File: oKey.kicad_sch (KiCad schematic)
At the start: 24 parts, among them P1 USB_C_Plug_USB2.0, SW1 SW_Push, U1 RP2350_60QFN, U2 NCP1117-3.3_SOT223, U3 W25Q128JVS

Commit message: minimal schematic
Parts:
- added C16, C17: 15p, symbol Device:C
- added C18: 4.7u, symbol Device:C
- added C19: C, symbol Device:C
- added L1: 3.3u, symbol Device:L
- added R4: 0, symbol Device:R
- added R6: DNF, symbol Device:R
- added R7, R8: 1K, symbol Device:R
- added R9: 33, symbol Device:R
- added SW2: SW_Push, symbol Switch:SW_Push
- added X1: ABM8-272-T3, ABM8-272-T3_ABR, symbol ABM8-272-T3:ABM8-272-T3
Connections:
- net GND is gone; now on net +3V3: C1.1, C10.2, C11.2, C12.2, C13.2, C14.2, C15.2, C2.1, C3.2, C4.2, C5.2, C6.2, C7.2, C8.2, C9.2, P1.A1 (GND), P1.A12 (GND), P1.B1 (GND), P1.B12 (GND), P1.S1 (SHIELD), R1.2, SW1.2, U1.1 (IOVDD), U1.11 (IOVDD), U1.20 (IOVDD), U1.30 (IOVDD), U1.38 (IOVDD), U1.44 (ADC_AVDD), U1.45 (IOVDD), U1.53 (USB_OTP_VDD), U1.54 (QSPI_IOVDD), U2.1 (GND), U3.4 (GND)
- net +1V1: now also U1.50 (VREG_FB), C19.1, L1.1
- net +3V3: now also U1.47 (VREG_PGND), U1.49 (VREG_VIN), U1.61 (GND), C16.2, C17.2, C18.1, C19.2, R6.1, R9.1, SW2.2, X1.2, X1.4
- net XIN: now reaches U1.21 (XIN)
- net XIN: now also C16.1, X1.1
- net XOUT: now reaches U1.22 (XOUT)
- net XOUT: now also R7.2
- net at U1.26 (RUN): now also R8.2
- net at U1.46 (VREG_AVDD): now also C18.2, R9.2
- net at U1.48 (VREG_LX): now also L1.2
- net QSPI_SS: now reaches R5.2, U1.60 (QSPI_SS)
- net QSPI_SS: now also R4.1
- net at U3.1 (~{CS}): now also R4.2, R6.2
- new net: C17.1, R7.1, X1.3
- new net: R8.1, SW2.1
- no-connect marks 0 -> 34
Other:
- note added: "12 MHz Crystal"
- note added: "RESET"
- note added: "pullup that this flash chip doesn't need"
- moved on the sheet: R5, SW1

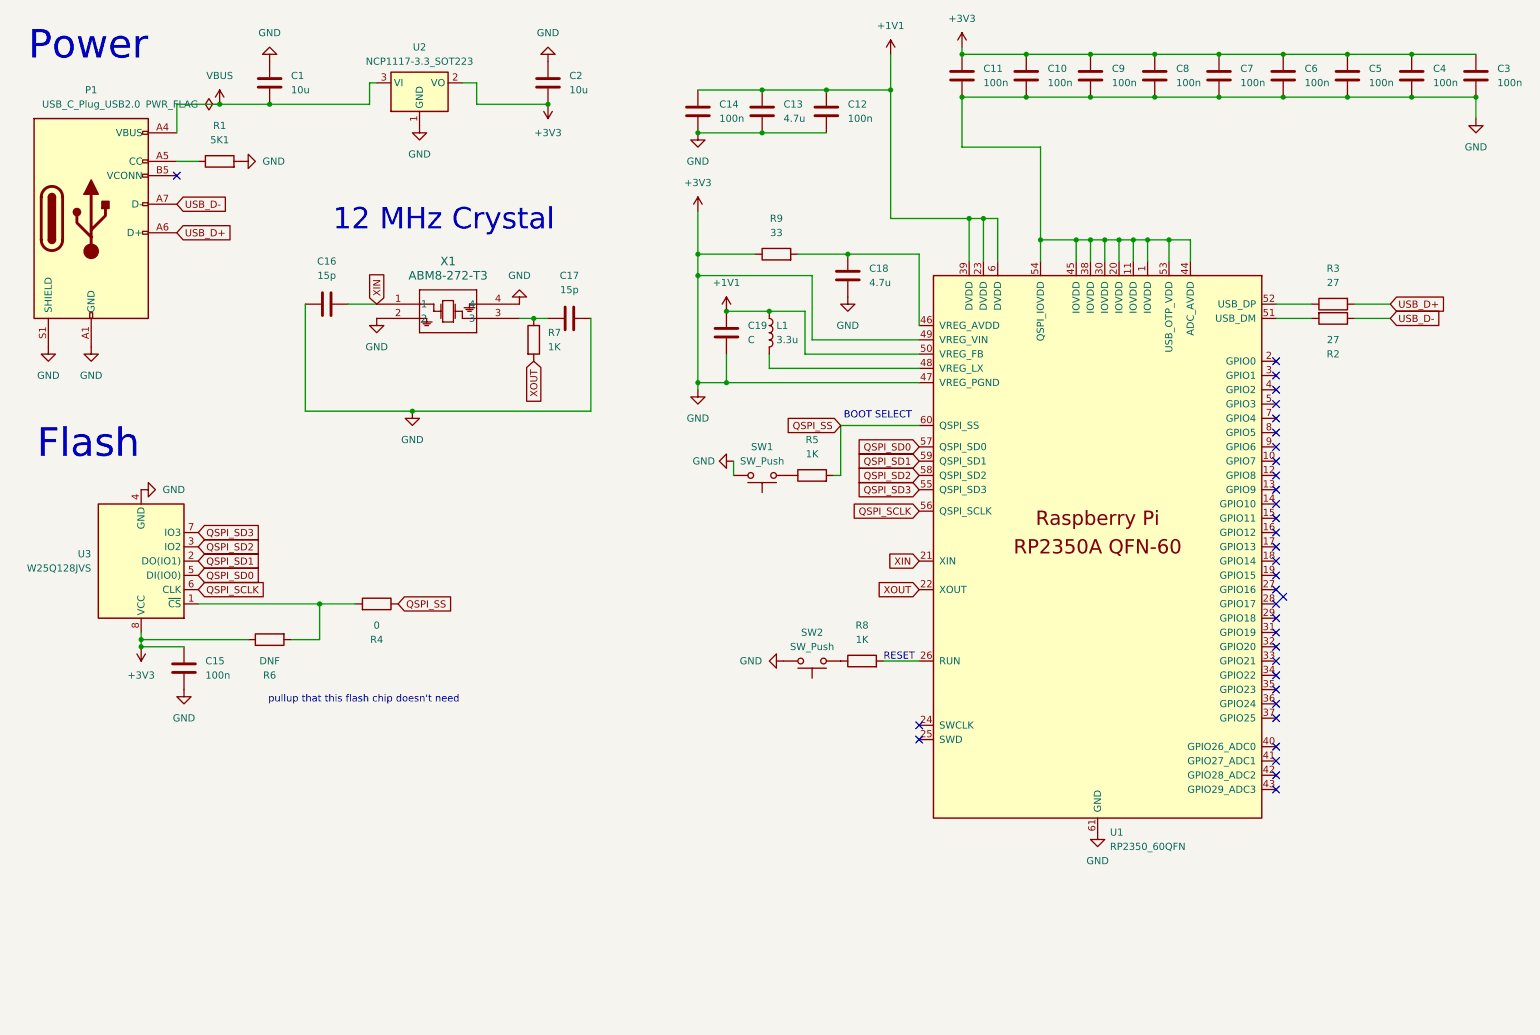
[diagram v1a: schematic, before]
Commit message: reorganise schematic and update images
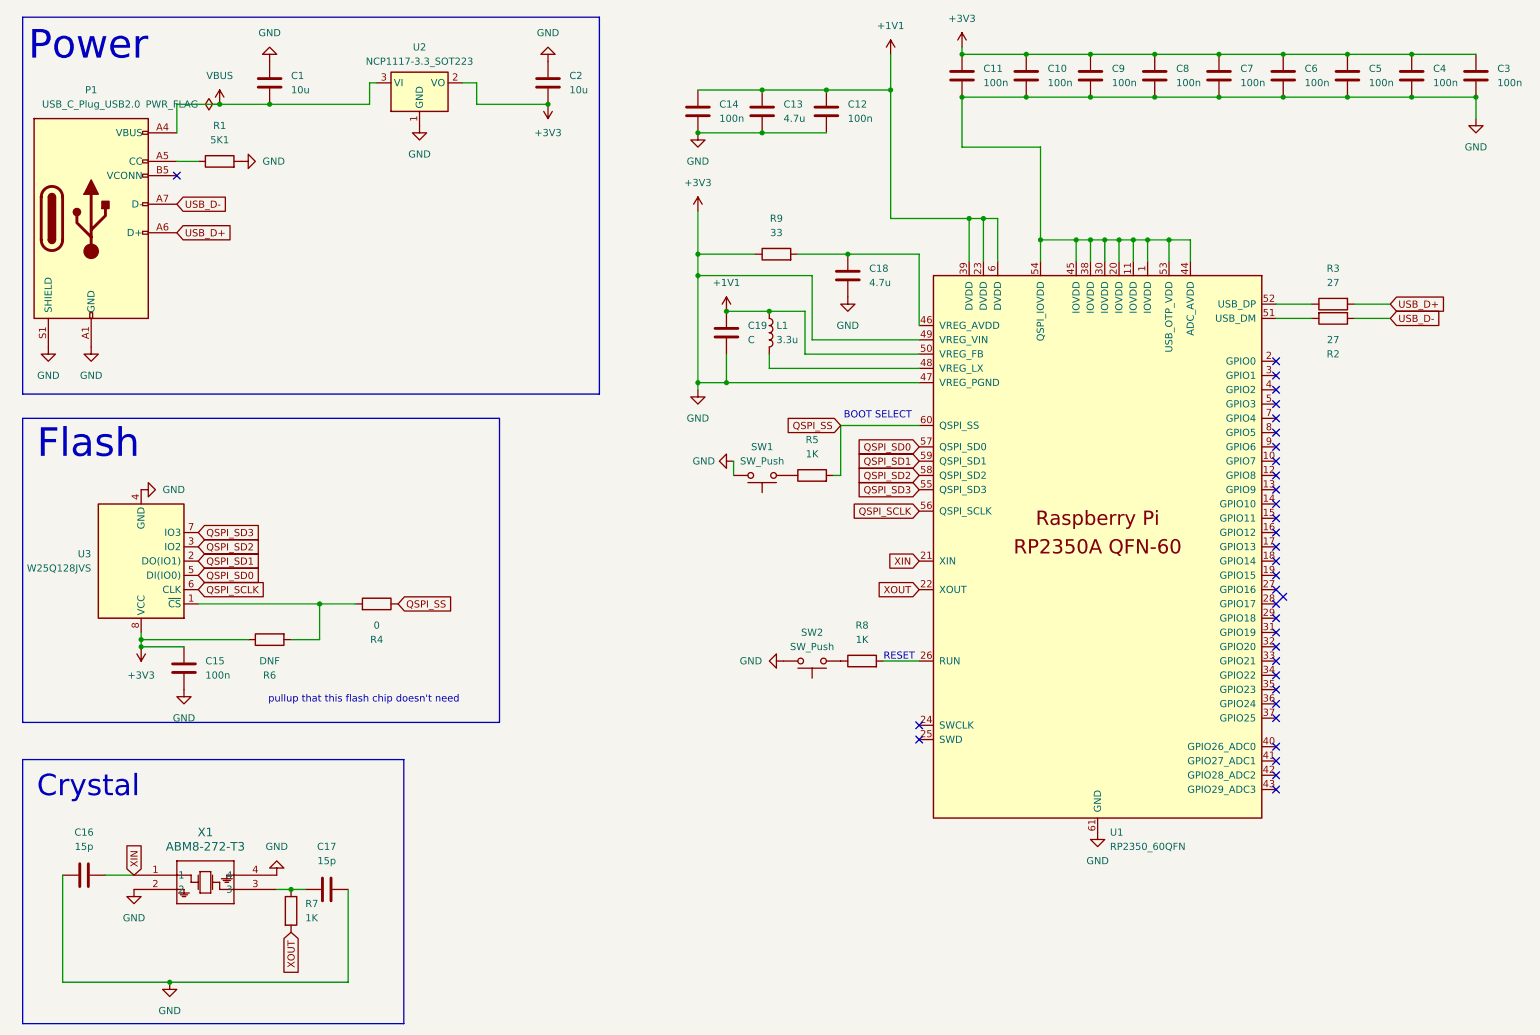
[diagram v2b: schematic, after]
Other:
- note added: "Crystal"
- note removed: "12 MHz Crystal"
- moved on the sheet: C16, C17, R7, X1
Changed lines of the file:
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@@
 	)
 	(junction
-		(at 105.41 68.58)
+		(at 62.23 170.18)
 		(diameter 0)
 		(color 0 0 0 0)
@@
 	)
 	(junction
-		(at 83.82 85.09)
+		(at 40.64 186.69)
 		(diameter 0)
 		(color 0 0 0 0)
@@
 	(wire
 		(pts
-			(xy 102.87 68.58) (xy 105.41 68.58)
+			(xy 59.69 170.18) (xy 62.23 170.18)
 		)
 		(stroke
@@
 	(wire
 		(pts
-			(xy 64.77 85.09) (xy 83.82 85.09)
+			(xy 21.59 186.69) (xy 40.64 186.69)
 		)
 		(stroke
@@
 	(wire
 		(pts
-			(xy 115.57 85.09) (xy 83.82 85.09)
+			(xy 72.39 186.69) (xy 40.64 186.69)
 		)
 		(stroke
@@
 	(wire
 		(pts
-			(xy 105.41 68.58) (xy 107.95 68.58)
+			(xy 62.23 170.18) (xy 64.77 170.18)
 		)
 		(stroke
@@
 	(wire
 		(pts
-			(xy 64.77 66.04) (xy 64.77 85.09)
+			(xy 21.59 167.64) (xy 21.59 186.69)
 		)
 		(stroke
@@
 	(wire
 		(pts
-			(xy 115.57 68.58) (xy 115.57 85.09)
+			(xy 72.39 170.18) (xy 72.39 186.69)
 		)
 		(stroke
@@
 	(wire
 		(pts
-			(xy 72.39 66.04) (xy 77.47 66.04)
+			(xy 29.21 167.64) (xy 34.29 167.64)
 		)
 		(stroke
@@
 		)
 	)
+	(rectangle
+		(start 14.478 14.986)
+		(end 117.094 82.042)
+		(stroke
+			(width 0)
+			(type default)
+		)
+		(fill
+			(type none)
+		)
+	)
+	(rectangle
+		(start 14.478 147.066)
+		(end 82.296 194.056)
+		(stroke
+			(width 0)
+			(type default)
+		)
+		(fill
+			(type none)
+		)
+	)
+	(rectangle
+		(start 14.478 86.36)
+		(end 99.314 140.462)
+		(stroke
+			(width 0)
+			(type default)
+		)
+		(fill
+			(type none)
+		)
+	)
 	(text "BOOT SELECT"
 		(exclude_from_sim no)
@@
 		)
 	)
-	(text "12 MHz Crystal"
+	(text "Crystal"
 		(exclude_from_sim no)
-		(at 89.408 51.054 0)
+		(at 26.162 151.892 0)
 		(effects
 			(font
@@
 	(global_label "XIN"
 		(shape input)
-		(at 77.47 66.04 90)
+		(at 34.29 167.64 90)
 		(fields_autoplaced yes)
 		(effects
@@
 		)
 		(property "Intersheetrefs" "${INTERSHEET_REFS}"
-			(at 77.47 59.91 90)
+			(at 34.29 161.51 90)
 			(effects
 				(font
@@
 	(global_label "XOUT"
 		(shape input)
-		(at 105.41 76.2 270)
+		(at 62.23 177.8 270)
 		(fields_autoplaced yes)
 		(effects
@@
 		)
 		(property "Intersheetrefs" "${INTERSHEET_REFS}"
-			(at 105.41 84.0233 90)
+			(at 62.23 185.6233 90)
 			(effects
 				(font
@@
 	(symbol
 		(lib_id "Device:R")
-		(at 105.41 72.39 0)
+		(at 62.23 173.99 0)
 		(unit 1)
 		(exclude_from_sim no)
@@
 		(fields_autoplaced yes)
 		(property "Reference" "R7"
-			(at 107.95 71.1199 0)
+			(at 64.77 172.7199 0)
 			(effects
 				(font
@@
 		)
 		(property "Value" "1K"
-			(at 107.95 73.6599 0)
+			(at 64.77 175.2599 0)
 			(effects
 				(font
@@
 		)
 		(property "Footprint" ""
-			(at 103.632 72.39 90)
+			(at 60.452 173.99 90)
 			(effects
 				(font
@@
 		)
 		(property "Datasheet" "~"
-			(at 105.41 72.39 0)
+			(at 62.23 173.99 0)
 			(effects
 				(font
@@
 		)
 		(property "Description" "Resistor"
-			(at 105.41 72.39 0)
+			(at 62.23 173.99 0)
 			(effects
 				(font
@@
 	(symbol
 		(lib_id "Device:C")
-		(at 68.58 66.04 270)
+		(at 25.4 167.64 270)
 		(unit 1)
 		(exclude_from_sim no)
@@
 		(fields_autoplaced yes)
 		(property "Reference" "C16"
-			(at 68.58 58.42 90)
+			(at 25.4 160.02 90)
 			(effects
 				(font
@@
 		)
 		(property "Value" "15p"
-			(at 68.58 60.96 90)
+			(at 25.4 162.56 90)
 			(effects
 				(font
@@
 		)
 		(property "Footprint" ""
-			(at 64.77 67.0052 0)
+			(at 21.59 168.6052 0)
 			(effects
 				(font
@@
 		)
 		(property "Datasheet" "~"
-			(at 68.58 66.04 0)
+			(at 25.4 167.64 0)
 			(effects
 				(font
@@
 		)
 		(property "Description" "Unpolarized capacitor"
-			(at 68.58 66.04 0)
+			(at 25.4 167.64 0)
 			(effects
 				(font
@@
 	(symbol
 		(lib_id "power:GND")
-		(at 77.47 68.58 0)
+		(at 34.29 170.18 0)
 		(unit 1)
 		(exclude_from_sim no)
@@
 		(fields_autoplaced yes)
 		(property "Reference" "#PWR017"
-			(at 77.47 74.93 0)
+			(at 34.29 176.53 0)
 			(effects
 				(font
@@
 		)
 		(property "Value" "GND"
-			(at 77.47 73.66 0)
+			(at 34.29 175.26 0)
 			(effects
 				(font
@@
 		)
 		(property "Footprint" ""
-			(at 77.47 68.58 0)
+			(at 34.29 170.18 0)
 			(effects
 				(font
@@
 		)
 		(property "Datasheet" ""
-			(at 77.47 68.58 0)
+			(at 34.29 170.18 0)
 			(effects
 				(font
@@
 		)
 		(property "Description" "Power symbol creates a global label with name \"GND\" , ground"
-			(at 77.47 68.58 0)
+			(at 34.29 170.18 0)
 			(effects
 				(font
@@
 	(symbol
 		(lib_id "power:GND")
-		(at 83.82 85.09 0)
+		(at 40.64 186.69 0)
 		(unit 1)
 		(exclude_from_sim no)
@@
 		(fields_autoplaced yes)
 		(property "Reference" "#PWR019"
-			(at 83.82 91.44 0)
+			(at 40.64 193.04 0)
 			(effects
 				(font
@@
 		)
 		(property "Value" "GND"
-			(at 83.82 90.17 0)
+			(at 40.64 191.77 0)
 			(effects
 				(font
@@
 		)
 		(property "Footprint" ""
-			(at 83.82 85.09 0)
+			(at 40.64 186.69 0)
 			(effects
 				(font
@@
 		)
 		(property "Datasheet" ""
-			(at 83.82 85.09 0)
+			(at 40.64 186.69 0)
 			(effects
 				(font
@@
 		)
 		(property "Description" "Power symbol creates a global label with name \"GND\" , ground"
-			(at 83.82 85.09 0)
+			(at 40.64 186.69 0)
 			(effects
 				(font
@@
 	(symbol
 		(lib_id "ABM8-272-T3:ABM8-272-T3")
-		(at 77.47 66.04 0)
+		(at 34.29 167.64 0)
 		(unit 1)
 		(exclude_from_sim no)
@@
 		(fields_autoplaced yes)
 		(property "Reference" "X1"
-			(at 90.17 58.42 0)
+			(at 46.99 160.02 0)
 			(effects
 				(font
@@
 		)
 		(property "Value" "ABM8-272-T3"
-			(at 90.17 60.96 0)
+			(at 46.99 162.56 0)
 			(effects
 				(font
@@
 		)
 		(property "Footprint" "ABM8-272-T3_ABR"
-			(at 77.47 66.04 0)
+			(at 34.29 167.64 0)
 			(effects
 				(font
@@
 		)
 		(property "Datasheet" "ABM8-272-T3"
-			(at 77.47 66.04 0)
+			(at 34.29 167.64 0)
 			(effects
 				(font
@@
 		)
 		(property "Description" ""
-			(at 77.47 66.04 0)
+			(at 34.29 167.64 0)
 			(effects
 				(font
@@
 	(symbol
 		(lib_id "Device:C")
-		(at 111.76 68.58 90)
+		(at 68.58 170.18 90)
 		(unit 1)
 		(exclude_from_sim no)
@@
 		(fields_autoplaced yes)
 		(property "Reference" "C17"
-			(at 111.76 60.96 90)
+			(at 68.58 162.56 90)
 			(effects
 				(font
@@
 		)
 		(property "Value" "15p"
-			(at 111.76 63.5 90)
+			(at 68.58 165.1 90)
 			(effects
 				(font
@@
 		)
 		(property "Footprint" ""
-			(at 115.57 67.6148 0)
+			(at 72.39 169.2148 0)
 			(effects
 				(font
@@
 		)
 		(property "Datasheet" "~"
-			(at 111.76 68.58 0)
+			(at 68.58 170.18 0)
 			(effects
 				(font
@@
 		)
 		(property "Description" "Unpolarized capacitor"
-			(at 111.76 68.58 0)
+			(at 68.58 170.18 0)
 			(effects
 				(font
@@
 	(symbol
 		(lib_id "power:GND")
-		(at 102.87 66.04 180)
+		(at 59.69 167.64 180)
 		(unit 1)
 		(exclude_from_sim no)
@@
 		(fields_autoplaced yes)
 		(property "Reference" "#PWR018"
-			(at 102.87 59.69 0)
+			(at 59.69 161.29 0)
 			(effects
 				(font
@@
 		)
 		(property "Value" "GND"
-			(at 102.87 60.96 0)
+			(at 59.69 162.56 0)
 			(effects
 				(font
@@
 		)
 		(property "Footprint" ""
-			(at 102.87 66.04 0)
+			(at 59.69 167.64 0)
 			(effects
 				(font
@@
 		)
 		(property "Datasheet" ""
-			(at 102.87 66.04 0)
+			(at 59.69 167.64 0)
 			(effects
 				(font
@@
 		)
 		(property "Description" "Power symbol creates a global label with name \"GND\" , ground"
-			(at 102.87 66.04 0)
+			(at 59.69 167.64 0)
 			(effects
 				(font
